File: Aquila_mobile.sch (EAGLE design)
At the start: 177 parts, among them J200 DNI, J201 DNI, J210 DNI, J220 DNI, J300 78646-3001, J310 U.FL_CONNECTOR, J400 10103593, K100 1376408-1_DDR1_1.8V_REDUCED, Q300 DTC143ZET1G, Q301 DTC143ZET1G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

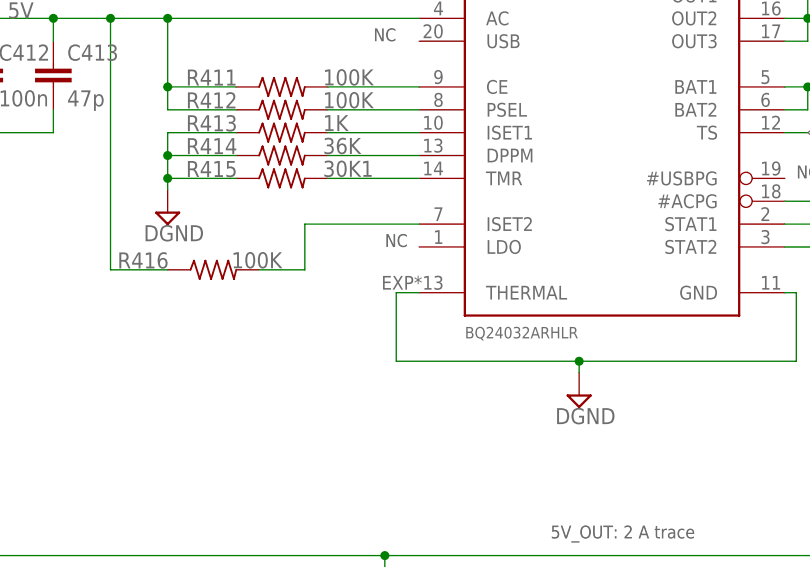
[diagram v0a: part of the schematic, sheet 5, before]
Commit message: Layout: fix errata into U410 and U420 pads
Pads from U410 and U420 designators didn't contain solder mask (tStop)
and stencil mask (tCream). This patch corrects designs files and gerbers.

Signed-off-by: Pau Pajuelo <ppajuel@gmail.com>
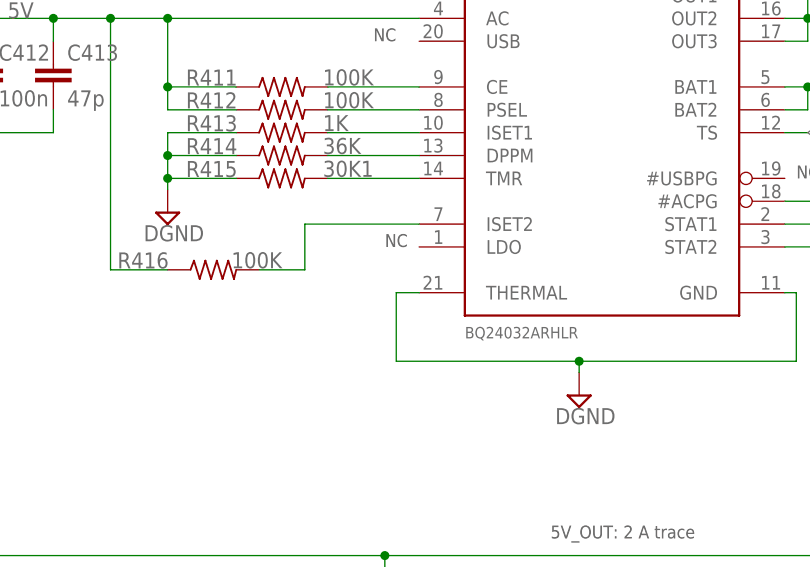
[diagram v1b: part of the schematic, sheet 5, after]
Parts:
- U410: device texas-MOD:BQ24032ARHLR -> ppajuel_library:BQ24032ARHLR
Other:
- moved on the sheet: U410
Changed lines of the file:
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@@
 <grid distance="0.1" unitdist="inch" unit="inch" style="lines" multiple="1" display="no" altdistance="0.01" altunitdist="inch" altunit="inch"/>
 <layers>
-<layer number="1" name="Top" color="4" fill="1" visible="no" active="no"/>
-<layer number="2" name="Route2" color="1" fill="3" visible="no" active="no"/>
-<layer number="3" name="Route3" color="4" fill="3" visible="no" active="no"/>
-<layer number="4" name="Route4" color="1" fill="4" visible="no" active="no"/>
-<layer number="5" name="Route5" color="4" fill="4" visible="no" active="no"/>
-<layer number="6" name="Route6" color="1" fill="8" visible="no" active="no"/>
-<layer number="7" name="Route7" color="4" fill="8" visible="no" active="no"/>
-<layer number="8" name="Route8" color="1" fill="2" visible="no" active="no"/>
-<layer number="9" name="Route9" color="4" fill="2" visible="no" active="no"/>
-<layer number="10" name="Route10" color="1" fill="7" visible="no" active="no"/>
-<layer number="11" name="Route11" color="4" fill="7" visible="no" active="no"/>
-<layer number="12" name="Route12" color="1" fill="5" visible="no" active="no"/>
-<layer number="13" name="Route13" color="4" fill="5" visible="no" active="no"/>
-<layer number="14" name="Route14" color="1" fill="6" visible="no" active="no"/>
-<layer number="15" name="Route15" color="4" fill="6" visible="no" active="no"/>
-<layer number="16" name="Bottom" color="1" fill="1" visible="no" active="no"/>
-<layer number="17" name="Pads" color="2" fill="1" visible="no" active="no"/>
-<layer number="18" name="Vias" color="2" fill="1" visible="no" active="no"/>
-<layer number="19" name="Unrouted" color="6" fill="1" visible="no" active="no"/>
-<layer number="20" name="Dimension" color="15" fill="1" visible="no" active="no"/>
-<layer number="21" name="tPlace" color="7" fill="1" visible="no" active="no"/>
-<layer number="22" name="bPlace" color="7" fill="1" visible="no" active="no"/>
-<layer number="23" name="tOrigins" color="15" fill="1" visible="no" active="no"/>
-<layer number="24" name="bOrigins" color="15" fill="1" visible="no" active="no"/>
-<layer number="25" name="tNames" color="7" fill="1" visible="no" active="no"/>
-<layer number="26" name="bNames" color="7" fill="1" visible="no" active="no"/>
-<layer number="27" name="tValues" color="7" fill="1" visible="no" active="no"/>
-<layer number="28" name="bValues" color="7" fill="1" visible="no" active="no"/>
+<layer number="1" name="Top" color="4" fill="1" visible="yes" active="no"/>
+<layer number="2" name="Route2" color="1" fill="3" visible="yes" active="no"/>
+<layer number="3" name="Route3" color="4" fill="3" visible="yes" active="no"/>
+<layer number="4" name="Route4" color="1" fill="4" visible="yes" active="no"/>
+<layer number="5" name="Route5" color="4" fill="4" visible="yes" active="no"/>
+<layer number="6" name="Route6" color="1" fill="8" visible="yes" active="no"/>
+<layer number="7" name="Route7" color="4" fill="8" visible="yes" active="no"/>
+<layer number="8" name="Route8" color="1" fill="2" visible="yes" active="no"/>
+<layer number="9" name="Route9" color="4" fill="2" visible="yes" active="no"/>
+<layer number="10" name="Route10" color="1" fill="7" visible="yes" active="no"/>
+<layer number="11" name="Route11" color="4" fill="7" visible="yes" active="no"/>
+<layer number="12" name="Route12" color="1" fill="5" visible="yes" active="no"/>
+<layer number="13" name="Route13" color="4" fill="5" visible="yes" active="no"/>
+<layer number="14" name="Route14" color="1" fill="6" visible="yes" active="no"/>
+<layer number="15" name="Route15" color="4" fill="6" visible="yes" active="no"/>
+<layer number="16" name="Bottom" color="1" fill="1" visible="yes" active="no"/>
+<layer number="17" name="Pads" color="2" fill="1" visible="yes" active="no"/>
+<layer number="18" name="Vias" color="2" fill="1" visible="yes" active="no"/>
+<layer number="19" name="Unrouted" color="6" fill="1" visible="yes" active="no"/>
+<layer number="20" name="Dimension" color="15" fill="1" visible="yes" active="no"/>
+<layer number="21" name="tPlace" color="7" fill="1" visible="yes" active="no"/>
+<layer number="22" name="bPlace" color="7" fill="1" visible="yes" active="no"/>
+<layer number="23" name="tOrigins" color="15" fill="1" visible="yes" active="no"/>
+<layer number="24" name="bOrigins" color="15" fill="1" visible="yes" active="no"/>
+<layer number="25" name="tNames" color="7" fill="1" visible="yes" active="no"/>
+<layer number="26" name="bNames" color="7" fill="1" visible="yes" active="no"/>
+<layer number="27" name="tValues" color="7" fill="1" visible="yes" active="no"/>
+<layer number="28" name="bValues" color="7" fill="1" visible="yes" active="no"/>
 <layer number="29" name="tStop" color="7" fill="3" visible="no" active="no"/>
 <layer number="30" name="bStop" color="7" fill="6" visible="no" active="no"/>
@@
 <layer number="35" name="tGlue" color="7" fill="4" visible="no" active="no"/>
 <layer number="36" name="bGlue" color="7" fill="5" visible="no" active="no"/>
-<layer number="37" name="tTest" color="7" fill="1" visible="no" active="no"/>
-<layer number="38" name="bTest" color="7" fill="1" visible="no" active="no"/>
+<layer number="37" name="tTest" color="7" fill="1" visible="yes" active="no"/>
+<layer number="38" name="bTest" color="7" fill="1" visible="yes" active="no"/>
 <layer number="39" name="tKeepout" color="4" fill="11" visible="no" active="no"/>
 <layer number="40" name="bKeepout" color="1" fill="11" visible="no" active="no"/>
@@
 <layer number="44" name="Drills" color="7" fill="1" visible="no" active="no"/>
 <layer number="45" name="Holes" color="7" fill="1" visible="no" active="no"/>
-<layer number="46" name="Milling" color="3" fill="1" visible="no" active="no"/>
-<layer number="47" name="Measures" color="7" fill="1" visible="no" active="no"/>
-<layer number="48" name="Document" color="7" fill="1" visible="no" active="no"/>
-<layer number="49" name="Reference" color="7" fill="1" visible="no" active="no"/>
-<layer number="50" name="dxf" color="7" fill="1" visible="no" active="no"/>
-<layer number="51" name="tDocu" color="7" fill="1" visible="no" active="no"/>
-<layer number="52" name="bDocu" color="7" fill="1" visible="no" active="no"/>
-<layer number="53" name="tGND_GNDA" color="7" fill="9" visible="no" active="no"/>
-<layer number="54" name="bGND_GNDA" color="1" fill="9" visible="no" active="no"/>
-<layer number="56" name="wert" color="7" fill="1" visible="no" active="no"/>
-<layer number="57" name="tCAD" color="7" fill="1" visible="no" active="no"/>
+<layer number="46" name="Milling" color="3" fill="1" visible="yes" active="no"/>
+<layer number="47" name="Measures" color="7" fill="1" visible="yes" active="no"/>
+<layer number="48" name="Document" color="7" fill="1" visible="yes" active="no"/>
+<layer number="49" name="Reference" color="7" fill="1" visible="yes" active="no"/>
+<layer number="50" name="dxf" color="7" fill="1" visible="yes" active="no"/>
+<layer number="51" name="tDocu" color="7" fill="1" visible="yes" active="no"/>
+<layer number="52" name="bDocu" color="7" fill="1" visible="yes" active="no"/>
+<layer number="53" name="tGND_GNDA" color="7" fill="9" visible="yes" active="no"/>
+<layer number="54" name="bGND_GNDA" color="1" fill="9" visible="yes" active="no"/>
+<layer number="56" name="wert" color="7" fill="1" visible="yes" active="no"/>
+<layer number="57" name="tCAD" color="7" fill="1" visible="yes" active="no"/>
 <layer number="91" name="Nets" color="2" fill="1" visible="yes" active="yes"/>
 <layer number="92" name="Busses" color="1" fill="1" visible="yes" active="yes"/>
@@
 <part name="D420" library="ppajuel_library" deviceset="STPS340U" device=""/>
 <part name="R420" library="rcl" deviceset="R-US_" device="R0402" value="0R"/>
-<part name="U410" library="texas-MOD" deviceset="BQ24032ARHLR" device=""/>
+<part name="U410" library="ppajuel_library" deviceset="BQ24032ARHLR" device=""/>
 <part name="U420" library="texas-MOD" deviceset="TPS6300*" device="" value="TPS63002DRC"/>
 <part name="L420" library="ppajuel_library" deviceset="SDR0403" device="" value="SDR0403-2R2ML"/>
